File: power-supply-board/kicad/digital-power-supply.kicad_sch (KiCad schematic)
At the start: 17 parts, among them J1 5V, J2 5V, J3 +12V, J4 +12V, J5 -12V, J6 -12V, SW1 SW, U1 USBC Module, U2 TPS5430 Module 5V, U3 TPS5430 Module 12V

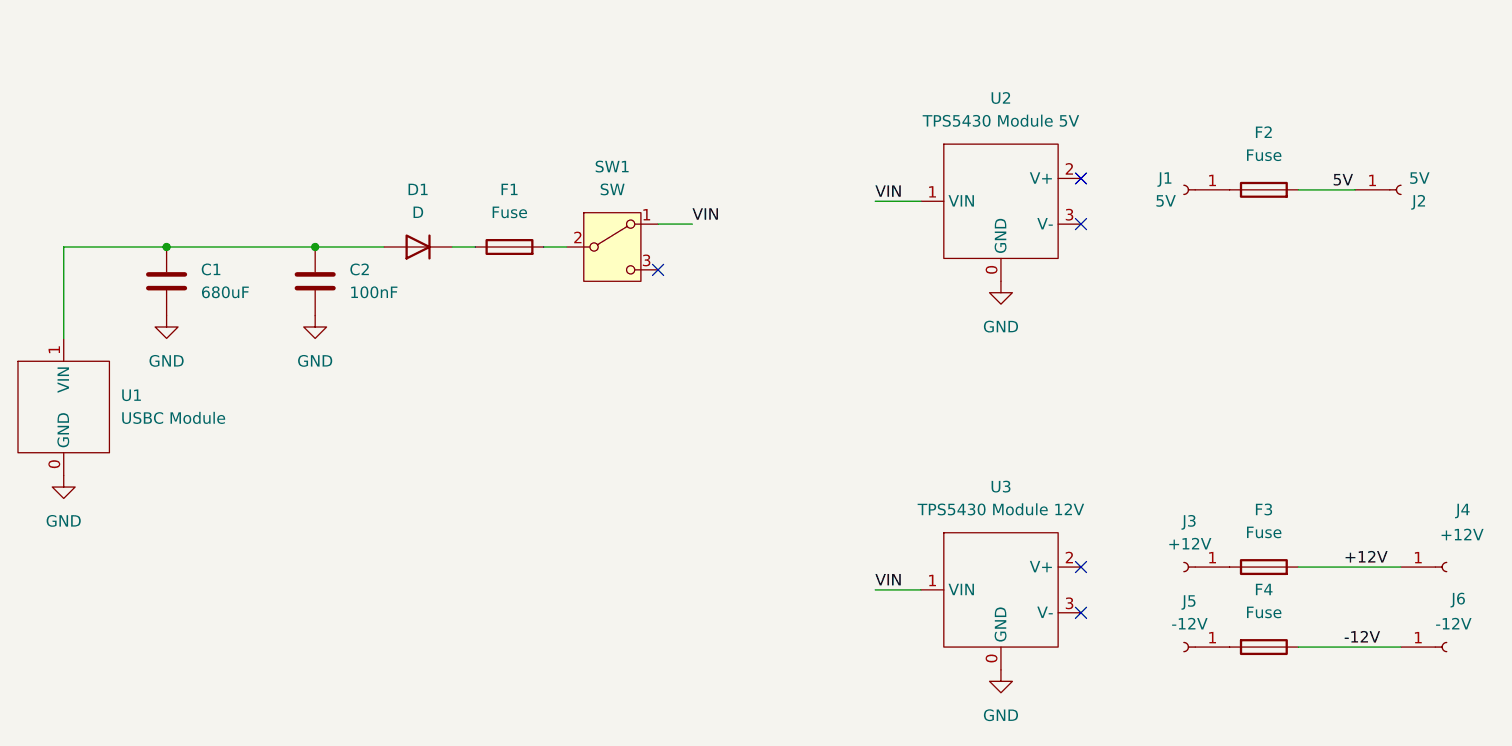
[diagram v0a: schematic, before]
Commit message: feat: new pcb design with crowbar overvoltage protection
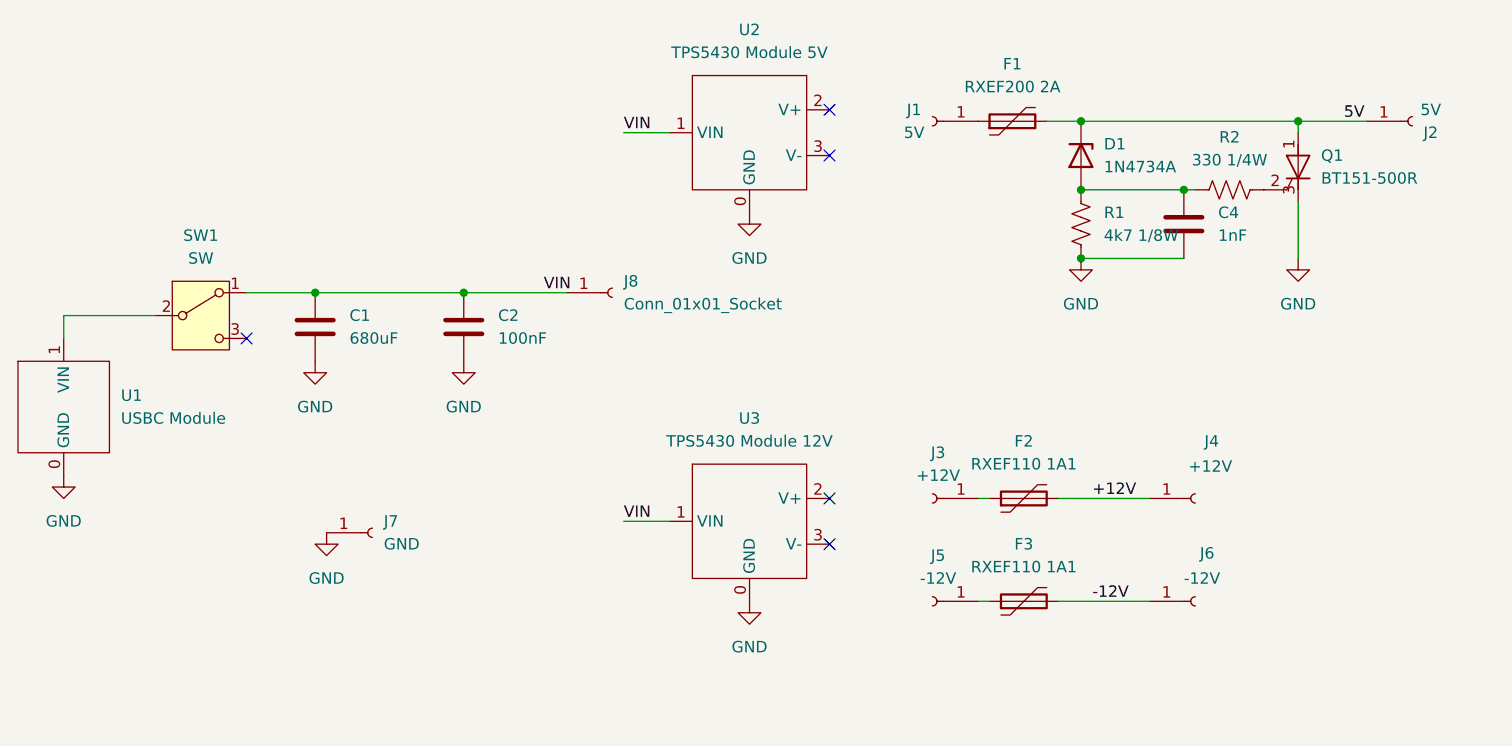
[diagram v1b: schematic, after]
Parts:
- removed D1: D, Diode_THT:D_A-405_P7.62mm_Horizontal, symbol Device:D
- removed F1, F2, F3, F4: Fuse, footprint:Fuse5x20mm, symbol Device:Fuse
- added C4: 1nF, Capacitor_THT:C_Disc_D3.0mm_W2.0mm_P2.50mm, symbol Device:C
- added D1: 1N4734A, Diode_THT:D_DO-34_SOD68_P7.62mm_Horizontal, symbol Device:D_Zener
- added F1: RXEF200 2A, Fuse:Fuse_Bourns_MF-RG300, symbol Device:Polyfuse
- added F2, F3: RXEF110 1A1, Fuse:Fuse_Bourns_MF-RG300, symbol Device:Polyfuse
- added J7: GND, footprints:Connector, symbol Connector:Conn_01x01_Socket
- added J8: Conn_01x01_Socket, footprints:Connector, symbol Connector:Conn_01x01_Socket
- added Q1: BT151-500R, Package_TO_SOT_THT:TO-92_Inline, symbol Triac_Thyristor:BT169B
- added R1: 4k7 1/8W, Resistor_THT:R_Axial_DIN0204_L3.6mm_D1.6mm_P5.08mm_Horizontal, symbol Device:R_US
- added R2: 330 1/4W, Resistor_THT:R_Axial_DIN0207_L6.3mm_D2.5mm_P10.16mm_Horizontal, symbol Device:R_US
- J1, J2, J3, J4, J5, J6: footprint footprint:SW -> footprints:Connector
- SW1: footprint footprint:SW -> (none)
- U1: footprint footprint:USBC_Module -> footprints:USBC_Module
- U2, U3: footprint footprint:TPS5430_Module -> footprints:TPS5430_Module
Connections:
- net +12V: now also F2.2
- net -12V: now also F3.2
- net 5V: now also D1.1 (K), F1.2, Q1.1 (A)
- net GND: now also C4.2, J7.1 (Pin_1), Q1.3 (K), R1.1
- net VIN: now also C1.1, C2.1, J8.1 (Pin_1)
- net at SW1.2 (B): now also U1.1 (VIN)
- net at J3.1 (Pin_1): now also F2.1
- net at J5.1 (Pin_1): now also F3.1
- net at J1.1 (Pin_1): now also F1.1
- new net: Q1.2 (G), R2.2
- new net: C4.1, D1.2 (A), R1.2, R2.1
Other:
- moved on the sheet: C1, C2, J1, J2, J3, J4, J5, J6, SW1, U2, U3

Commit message: feat: increase tracks width and add zone rules
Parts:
- added J9: 5V, footprints:Connector, symbol Connector:Conn_01x01_Socket
- J7: footprint footprints:Connector -> footprints:ConnectorGND
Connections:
- net 5V: now also J9.1 (Pin_1)
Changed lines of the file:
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@@
+	)
+	(junction
+		(at 187.96 57.15)
+		(diameter 0)
+		(color 0 0 0 0)
 	)
 	(junction
@@
 	(wire
 		(pts
-			(xy 180.34 64.77) (xy 191.77 64.77)
+			(xy 187.96 57.15) (xy 204.47 57.15)
 		)
 		(stroke
@@
 	(wire
 		(pts
-			(xy 176.53 57.15) (xy 180.34 57.15)
+			(xy 180.34 64.77) (xy 191.77 64.77)
 		)
 		(stroke
@@
 	(wire
 		(pts
-			(xy 67.31 78.74) (xy 67.31 81.28)
+			(xy 176.53 57.15) (xy 180.34 57.15)
 		)
 		(stroke
@@
 	(wire
 		(pts
-			(xy 204.47 57.15) (xy 212.09 57.15)
+			(xy 67.31 78.74) (xy 67.31 81.28)
 		)
 		(stroke
@@
 	(wire
 		(pts
-			(xy 177.8 110.49) (xy 187.96 110.49)
+			(xy 204.47 57.15) (xy 212.09 57.15)
 		)
 		(stroke
@@
 	(wire
 		(pts
-			(xy 177.8 99.06) (xy 187.96 99.06)
+			(xy 177.8 110.49) (xy 187.96 110.49)
 		)
 		(stroke
@@
 	(wire
 		(pts
-			(xy 180.34 57.15) (xy 204.47 57.15)
+			(xy 177.8 99.06) (xy 187.96 99.06)
+		)
+		(stroke
+			(width 0)
+			(type default)
+		)
+	)
+	(wire
+		(pts
+			(xy 180.34 57.15) (xy 187.96 57.15)
 		)
 		(stroke
@@
 			)
 		)
-		(property "Footprint" "footprints:Connector"
+		(property "Footprint" "footprints:ConnectorGND"
 			(at 101.6 102.87 0)
 			(hide yes)
@@
 					(unit 1)
 				)
+			)
+		)
+	)
+	(symbol
+		(lib_id "Connector:Conn_01x01_Socket")
+		(at 187.96 52.07 90)
+		(unit 1)
+		(body_style 1)
+		(exclude_from_sim no)
+		(in_bom yes)
+		(on_board yes)
+		(in_pos_files yes)
+		(dnp no)
+		(fields_autoplaced yes)
+		(property "Reference" "J9"
+			(at 189.23 51.4349 90)
+			(show_name no)
+			(do_not_autoplace no)
+			(effects
+				(font
+					(size 1.27 1.27)
+				)
+				(justify right)
+			)
+		)
+		(property "Value" "5V"
+			(at 189.23 53.9749 90)
+			(show_name no)
+			(do_not_autoplace no)
+			(effects
+				(font
+					(size 1.27 1.27)
+				)
+				(justify right)
+			)
+		)
+		(property "Footprint" "footprints:Connector"
+			(at 187.96 52.07 0)
+			(hide yes)
+			(show_name no)
+			(do_not_autoplace no)
+			(effects
+				(font
+					(size 1.27 1.27)
+				)
+			)
+		)
+		(property "Datasheet" ""
+			(at 187.96 52.07 0)
+			(hide yes)
+			(show_name no)
+			(do_not_autoplace no)
+			(effects
+				(font
+					(size 1.27 1.27)
+				)
+			)
+		)
+		(property "Description" "Generic connector, single row, 01x01, script generated"
+			(at 187.96 52.07 0)
+			(hide yes)
+			(show_name no)
+			(do_not_autoplace no)
+			(effects
+				(font
+					(size 1.27 1.27)
+				)
+			)
+		)
+		(pin "1"
+		)
+		(instances
+			(project "digital-power-supply"
+				(path "/76a99488-02db-4061-8b77-793475fd359a"
+					(reference "J9")
+					(unit 1)
+				)
